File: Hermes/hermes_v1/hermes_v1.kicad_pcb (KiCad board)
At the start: 2 copper layers, 100.6 x 59.7 mm, 83 parts, among them IC1 LD39200PU33R, J1 XT60-M, J2 FCC_BOOTSEL, J3 FCC_RESET, J4 5V_EXT_IN, J5 GND_EXT_IN, J6 2.54mm, J7 Conn_02x06_Odd_Even, J8 Connector_USB_B_Micro, U1 RP2040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

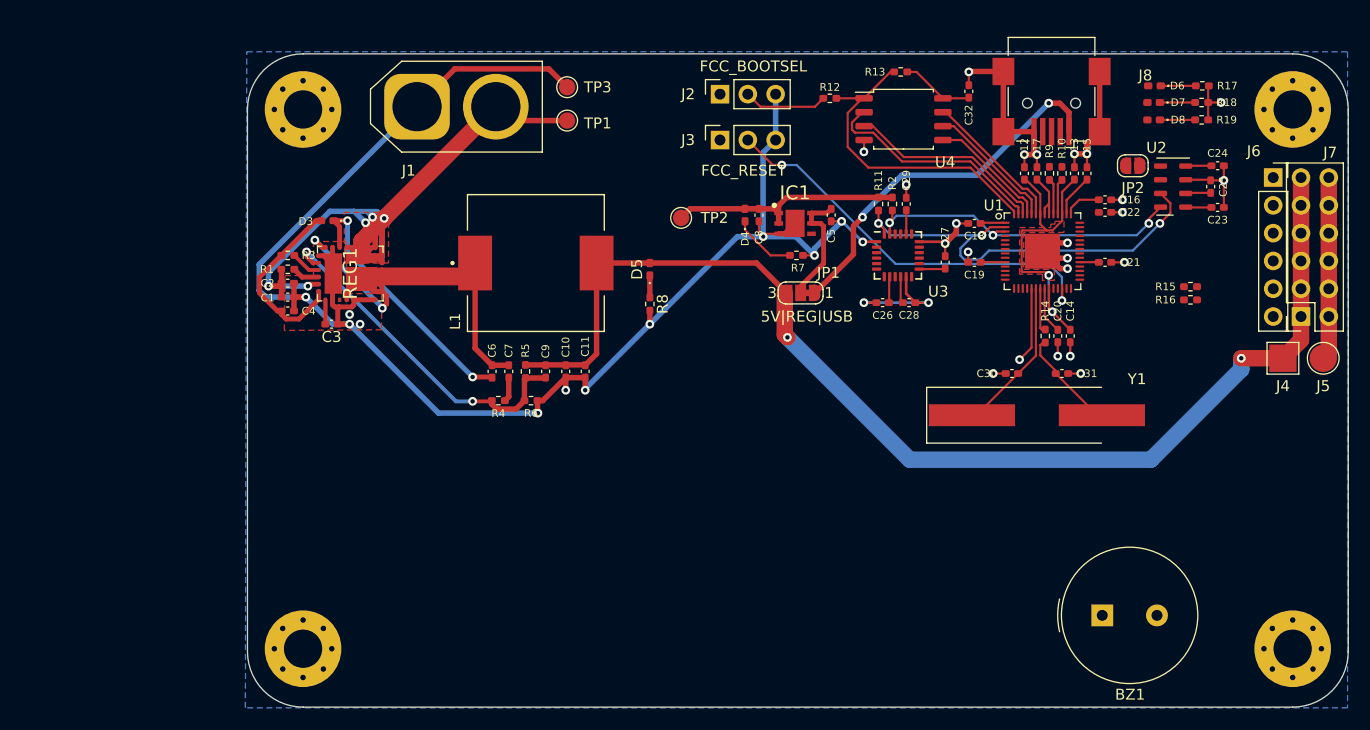
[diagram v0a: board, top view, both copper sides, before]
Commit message: changed board to pi-zero HAT design
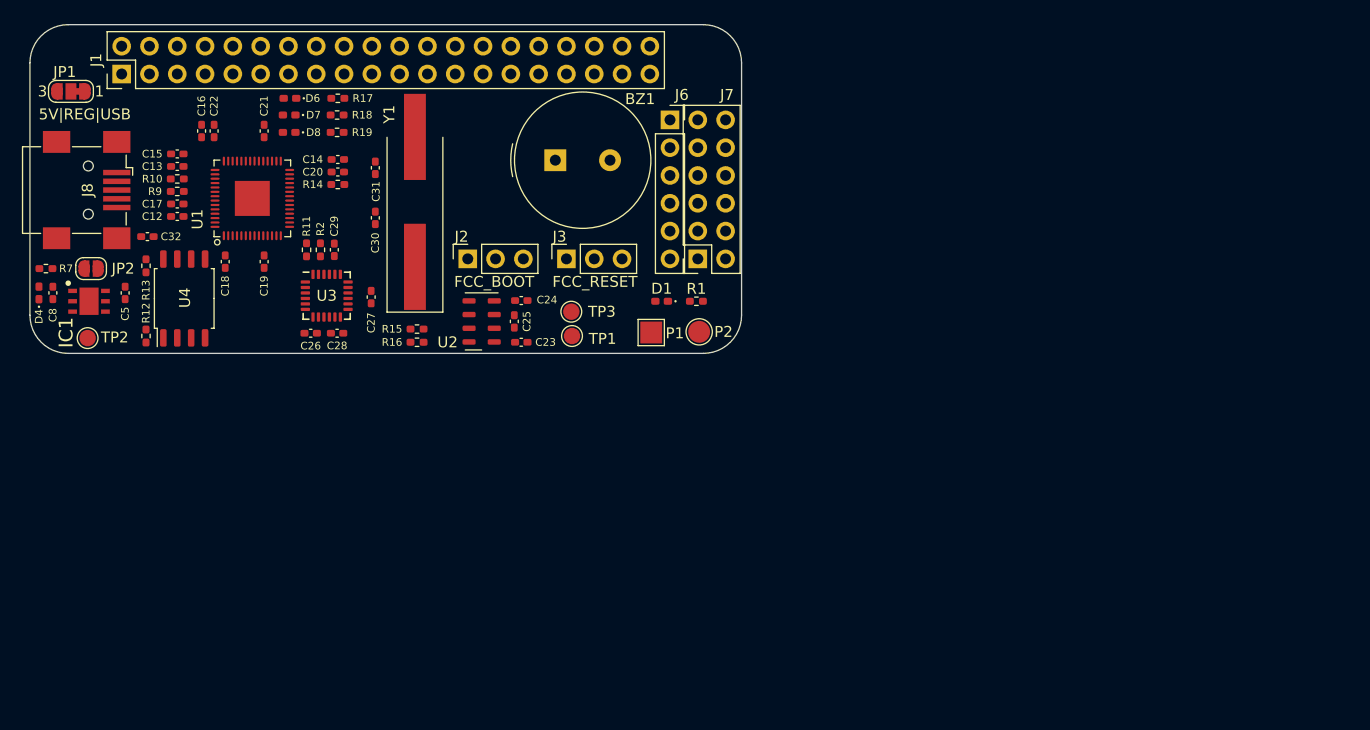
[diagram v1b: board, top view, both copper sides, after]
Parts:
- removed C1, C10: 100u, Capacitor_SMD:C_0402_1005Metric_Pad0.74x0.62mm_HandSolder
- removed C11, C2: 47u, Capacitor_SMD:C_0402_1005Metric_Pad0.74x0.62mm_HandSolder
- removed C3, C4: 2u2, Capacitor_SMD:C_0402_1005Metric_Pad0.74x0.62mm_HandSolder
- removed C6, C7: 100n, Capacitor_SMD:C_0402_1005Metric_Pad0.74x0.62mm_HandSolder
- removed C9: 4n7, Capacitor_SMD:C_0402_1005Metric_Pad0.74x0.62mm_HandSolder
- removed D3: SD103AWS, Diode_SMD:D_0402_1005Metric_Pad0.77x0.64mm_HandSolder
- removed D5: LED_G_5V, LED_SMD:LED_0402_1005Metric_Pad0.77x0.64mm_HandSolder
- removed J4: 5V_EXT_IN, TestPoint:TestPoint_Pad_2.5x2.5mm
- removed J5: GND_EXT_IN, TestPoint:TestPoint_Pad_D2.5mm
- removed L1: 15u, SRP1265A-330M:IND_SRP1265A-330M
- removed R3: 10k, Resistor_SMD:R_0402_1005Metric_Pad0.72x0.64mm_HandSolder
- removed R4: 19k6, Resistor_SMD:R_0402_1005Metric_Pad0.72x0.64mm_HandSolder
- removed R5: 6k8, Resistor_SMD:R_0402_1005Metric_Pad0.72x0.64mm_HandSolder
- removed R6: 1k3, Resistor_SMD:R_0402_1005Metric_Pad0.72x0.64mm_HandSolder
- removed R8: 560, Resistor_SMD:R_0402_1005Metric_Pad0.72x0.64mm_HandSolder
- removed REF** (x4): MountingHole_3.5mm_Pad_Via, MountingHole:MountingHole_3.5mm_Pad_Via
- removed REG1: MIC26903YJL-TR, SamacSys_Parts:MIC24054YJLTR
- added D1: LED_Small, LED_SMD:LED_0402_1005Metric_Pad0.77x0.64mm_HandSolder, F.Cu at (169.4, 77.5)
- added P1: 5V_BAT, TestPoint:TestPoint_Pad_2.0x2.0mm, F.Cu at (168.5, 80.3)
- added P2: GND_BAT, TestPoint:TestPoint_Pad_D2.0mm, F.Cu at (172.8, 80.3)
- J1: value XT60-M -> Raspberry Pi Zero; footprint Connector_AMASS:AMASS_XT60-F_1x02_P7.20mm_Vertical -> Connector_PinHeader_2.54mm:PinHeader_2x20_P2.54mm_Vertical
- J2: value FCC_BOOTSEL -> FCC_BOOT
- R1: value 10k -> 240
- TP1: value TestPoint_Probe -> 5V_BAT_Probe
- TP2: value TestPoint_Probe -> 3V3_Probe
- TP3: value TestPoint_Probe -> GND_BAT_Probe
- moved JP2 95.6 mm to (117.3, 74.5)
- moved J8 88.4 mm to (117.0, 67.3), turned to 270 degrees
- moved C15 83.1 mm to (125.2, 64.0), turned to 180 degrees
- moved C16 82.8 mm to (127.4, 61.9), turned to 90 degrees
- moved C13 82.0 mm to (125.2, 65.2), turned to 180 degrees
- moved C22 81.7 mm to (128.5, 61.9), turned to 90 degrees
- moved R10 80.8 mm to (125.2, 66.3), turned to 0 degrees
- moved R9 79.7 mm to (125.2, 67.4), turned to 0 degrees
- moved D6 79.0 mm to (135.5, 58.9)
- moved D7 79.0 mm to (135.4, 60.5)
- moved D8 79.0 mm to (135.4, 62.0)
- moved R17 79.0 mm to (139.8, 58.9)
- moved R18 79.0 mm to (139.8, 60.5)
- moved R19 79.0 mm to (139.8, 62.0)
- moved C17 78.6 mm to (125.2, 68.6), turned to 180 degrees
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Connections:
- C5 pad 1: REG_5VIN -> PI_5V
- IC1 pad 5: REG_5VIN -> PI_5V
- IC1 pad 6: REG_5VIN -> PI_5V
- J1 pad 1: GND -> Net-(J1-Pad1)
- J1 pad 2: REG_VIN -> PI_5V
- JP1 pad 2: REG_5VIN -> PI_5V
- R1 pad 1: REG_EN -> +5V
- R1 pad 2: REG_VIN -> Net-(D1-Pad1)
- TP1 pad 1: REG_VIN -> VCC
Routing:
- net GND: track 257.4 -> 0.00 mm, vias 37 -> 0
- net REG_VIN: track 121.3 -> 0.00 mm, vias 5 -> 0
- net +5V: track 109.4 -> 0.00 mm, vias 2 -> 0
- net REG_CS: track 54.2 -> 0.00 mm, vias 2 -> 0
- net FC_I2C0_SDA: track 41.1 -> 0.00 mm, vias 3 -> 0
- net +3V3: track 37.9 -> 0.00 mm
- net FC_RUN: track 37.1 -> 0.00 mm, vias 2 -> 0
- net FC_USB_VBUS: track 34.2 -> 0.00 mm, vias 2 -> 0
- net REG_FB: track 32.2 -> 0.00 mm, vias 2 -> 0
- net FC_I2C0_SCL: track 30.6 -> 0.00 mm, vias 3 -> 0
- net FC_QSPI_SS: track 29.3 -> 0.00 mm
- net +1V1: track 28.3 -> 0.00 mm, vias 2 -> 0
- net REG_BST: track 24.8 -> 0.00 mm, vias 2 -> 0
- net Net-(C15-Pad1): track 22.5 -> 0.00 mm
- net FC_QSPI_SD1: track 20.9 -> 0.00 mm
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- removed copper zone on F.Cu, net +1V1
- removed copper zone on B.Cu, net GND
- removed copper zone on F.Cu, net GND
- removed copper zone on F.Cu, net REG_VIN
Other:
- board size 100.6 x 59.7 mm -> 65 x 30 mm

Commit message: new
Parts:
- moved C18 0.38 mm to (129.5, 74.2)
- moved C19 0.38 mm to (133.1, 74.2)
- moved C12 0.13 mm to (125.3, 69.7)
- moved C13 0.13 mm to (125.3, 65.2)
- moved C15 0.13 mm to (125.3, 64.0)
- moved C17 0.13 mm to (125.3, 68.6)
- moved R10 0.13 mm to (125.3, 66.3)
- moved R9 0.13 mm to (125.3, 67.4)
- moved C16 0.09 mm to (127.3, 62.0)
- moved C21 0.09 mm to (133.0, 62.0)
- moved C22 0.09 mm to (128.5, 62.0)
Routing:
- net Net-(C15-Pad1): track 0.00 -> 44.4 mm, vias 0 -> 5
- net +1V1: track 0.00 -> 25.0 mm
- net FC_XIN: track 0.00 -> 14.6 mm
- net Net-(C31-Pad1): track 0.00 -> 8.38 mm
- net FC_XOUT: track 0.00 -> 4.41 mm

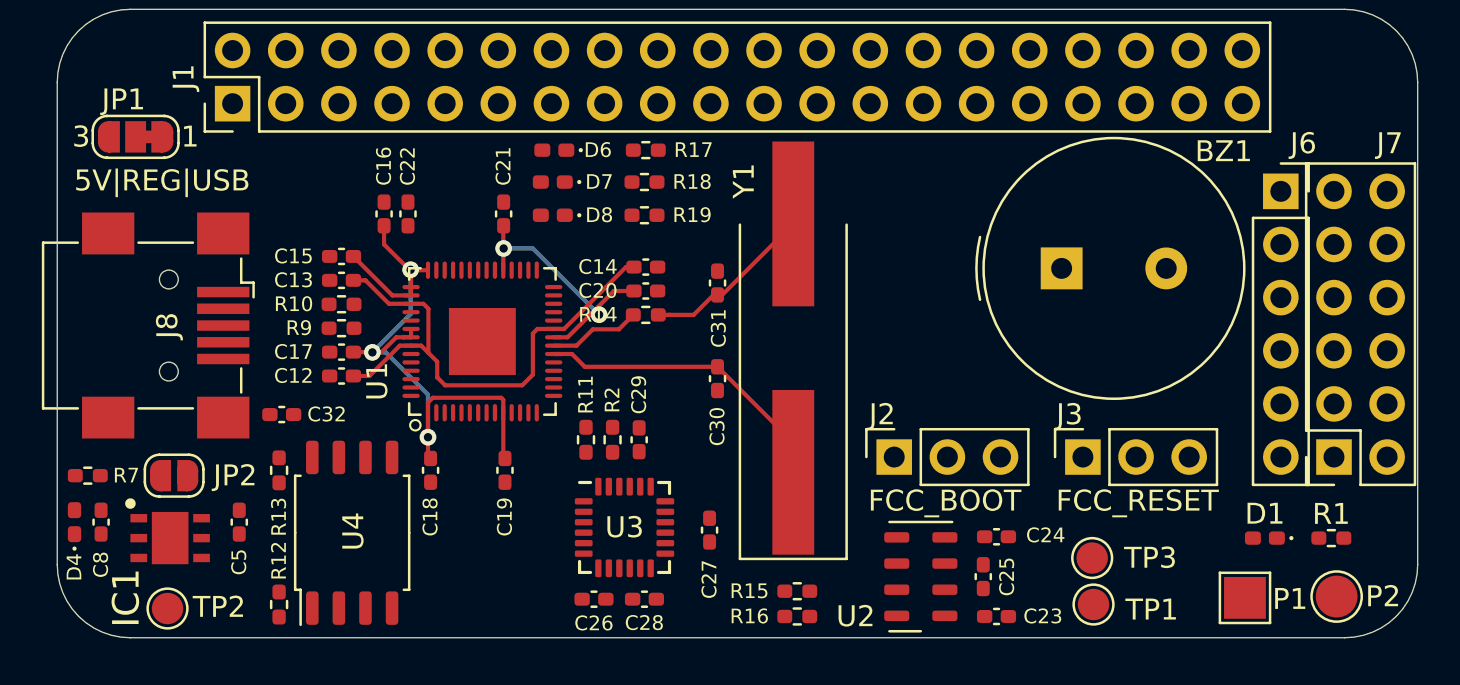
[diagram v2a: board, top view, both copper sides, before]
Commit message: routed rp2040
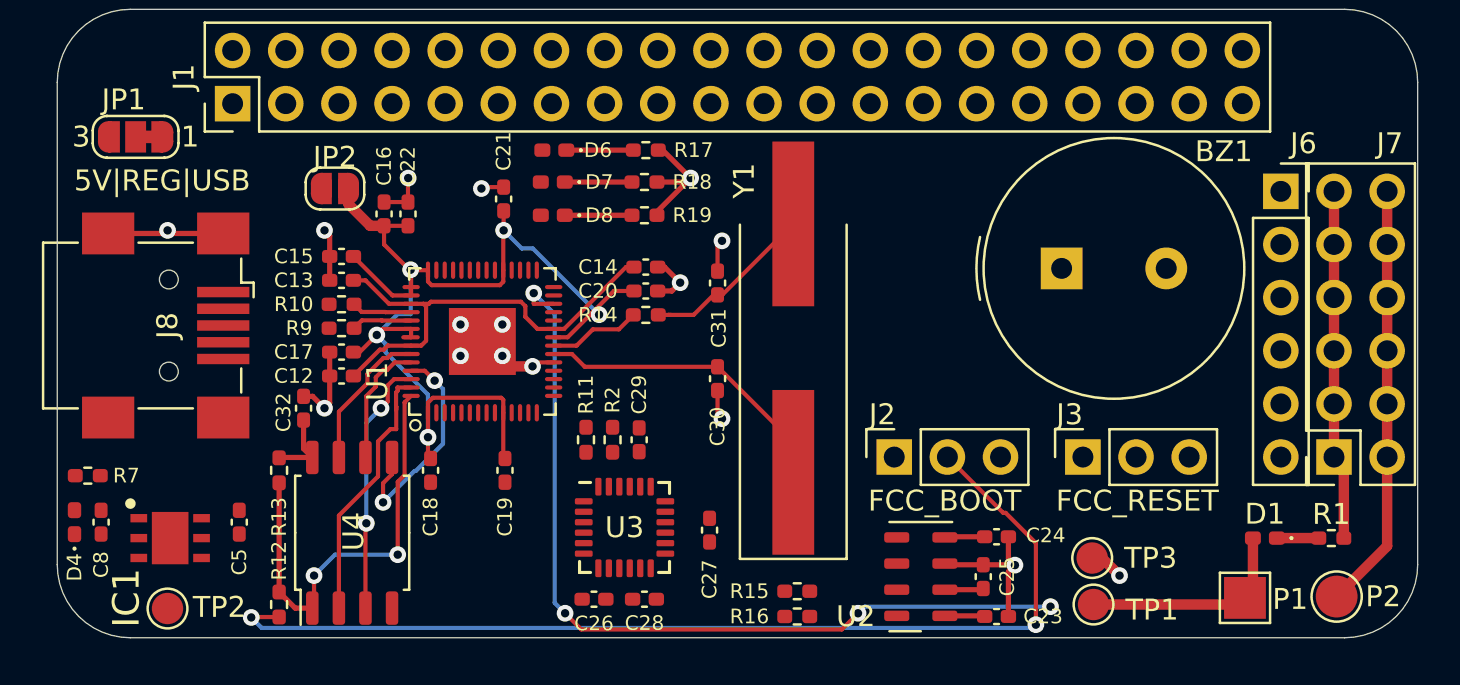
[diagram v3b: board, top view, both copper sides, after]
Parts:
- moved JP2 15.7 mm to (125.0, 60.8)
- moved C32 1.09 mm to (123.5, 71.3), turned to 90 degrees
- moved C21 0.71 mm to (133.0, 61.3)
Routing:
- net GND: track 0.00 -> 61.0 mm, vias 0 -> 16
- net FC_BOOTSEL: track 0.00 -> 49.0 mm, vias 0 -> 2
- net FC_RUN: track 0.00 -> 41.4 mm, vias 0 -> 4
- net FC_QSPI_SS: track 0.00 -> 21.0 mm, vias 0 -> 2
- net +5V: track 0.00 -> 16.8 mm
- net FC_QSPI_SD1: track 0.00 -> 12.7 mm
- net FC_QSPI_SD2: track 0.00 -> 12.3 mm, vias 0 -> 2
- net FC_QSPI_SD0: track 0.00 -> 10.9 mm, vias 0 -> 2
- net VCC: track 0.00 -> 10.4 mm
- net Net-(C15-Pad1): track 44.4 -> 54.6 mm
- net +3V3: track 0.00 -> 7.38 mm
- net FC_QSPI_SD3: track 0.00 -> 7.04 mm
- net FC_QSPI_SCLK: track 0.00 -> 6.02 mm
- net Net-(D8-Pad1): track 0.00 -> 3.21 mm
- net Net-(D7-Pad1): track 0.00 -> 3.21 mm
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
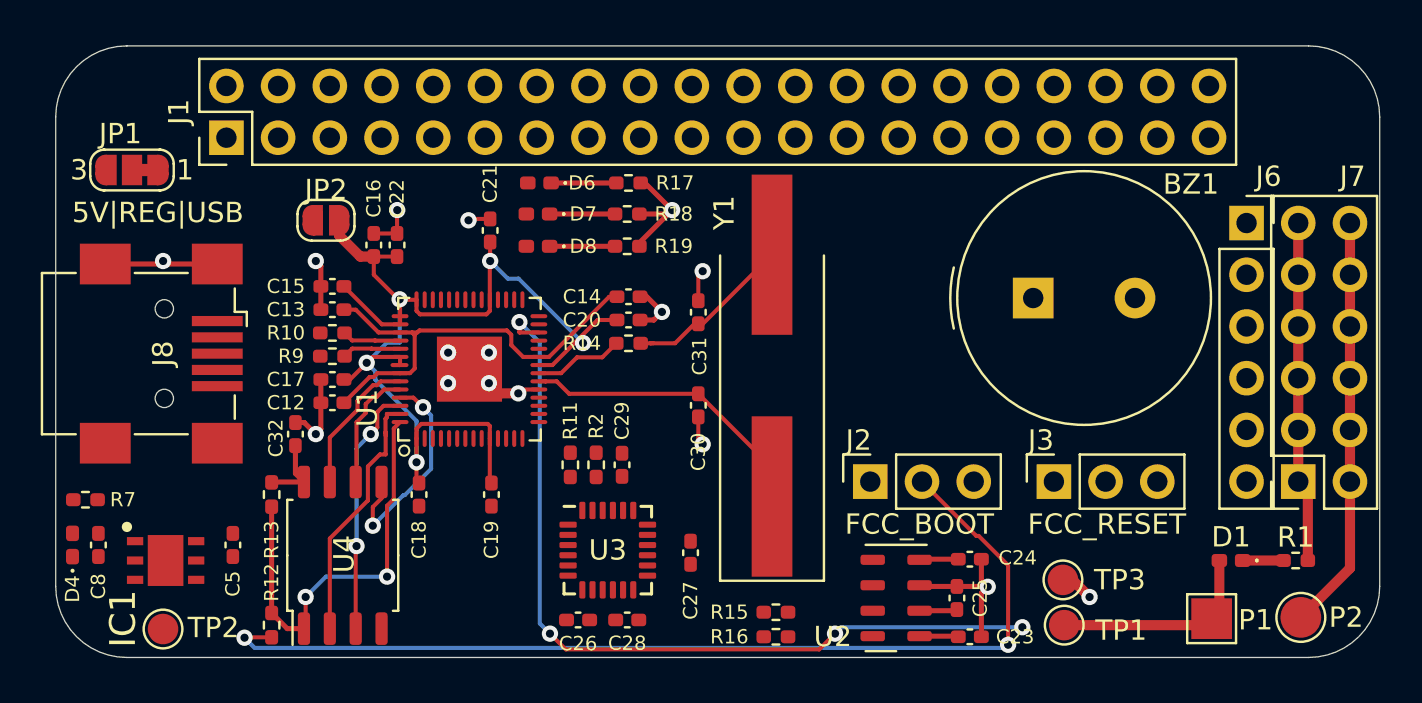
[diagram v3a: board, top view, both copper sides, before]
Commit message: added GND & 3V3 copper pours
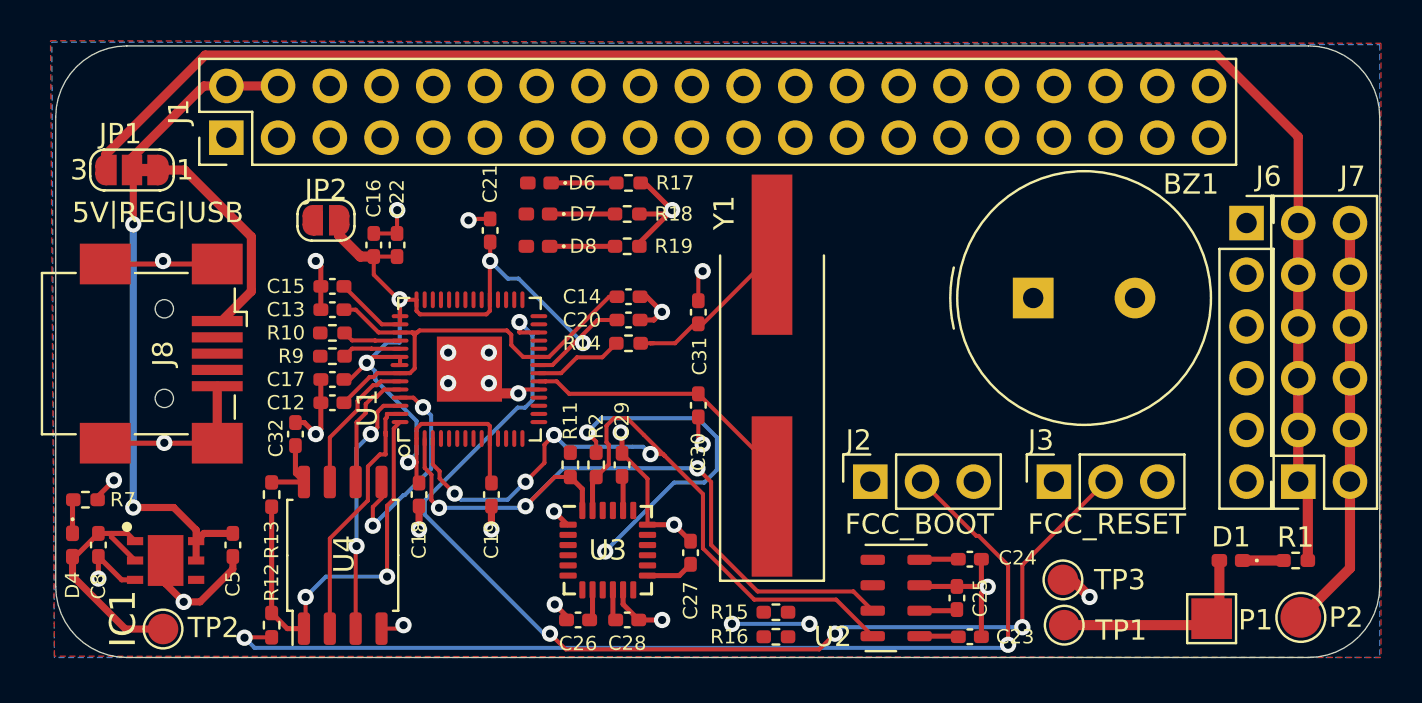
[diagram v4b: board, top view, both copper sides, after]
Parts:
- turned D4 to 270 degrees
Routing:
- net +5V: track 16.8 -> 84.0 mm
- net FC_I2C0_SCL: track 0.00 -> 39.6 mm, vias 0 -> 4
- net +3V3: track 7.38 -> 44.0 mm, vias 0 -> 4
- net FC_I2C0_SDA: track 0.00 -> 35.2 mm, vias 0 -> 3
- net GND: track 61.0 -> 95.9 mm, vias 16 -> 28
- net PI_5V: track 0.00 -> 32.8 mm, vias 0 -> 2
- net FC_RUN: track 41.4 -> 55.0 mm
- net FC_USB_VBUS: track 0.00 -> 10.9 mm
- net Net-(C29-Pad1): track 0.00 -> 1.69 mm
- net Net-(D4-Pad1): track 0.00 -> 1.67 mm
- net Net-(C28-Pad1): track 0.00 -> 1.53 mm
- net Net-(C15-Pad1): track 54.6 -> 55.2 mm
- added copper zone on F.Cu, net +3V3
- added copper zone on B.Cu, net GND
